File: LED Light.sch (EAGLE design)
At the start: 13 parts, among them J1 AVR_SPI_PRG_6NS, U1 Tiny85-20-SMT

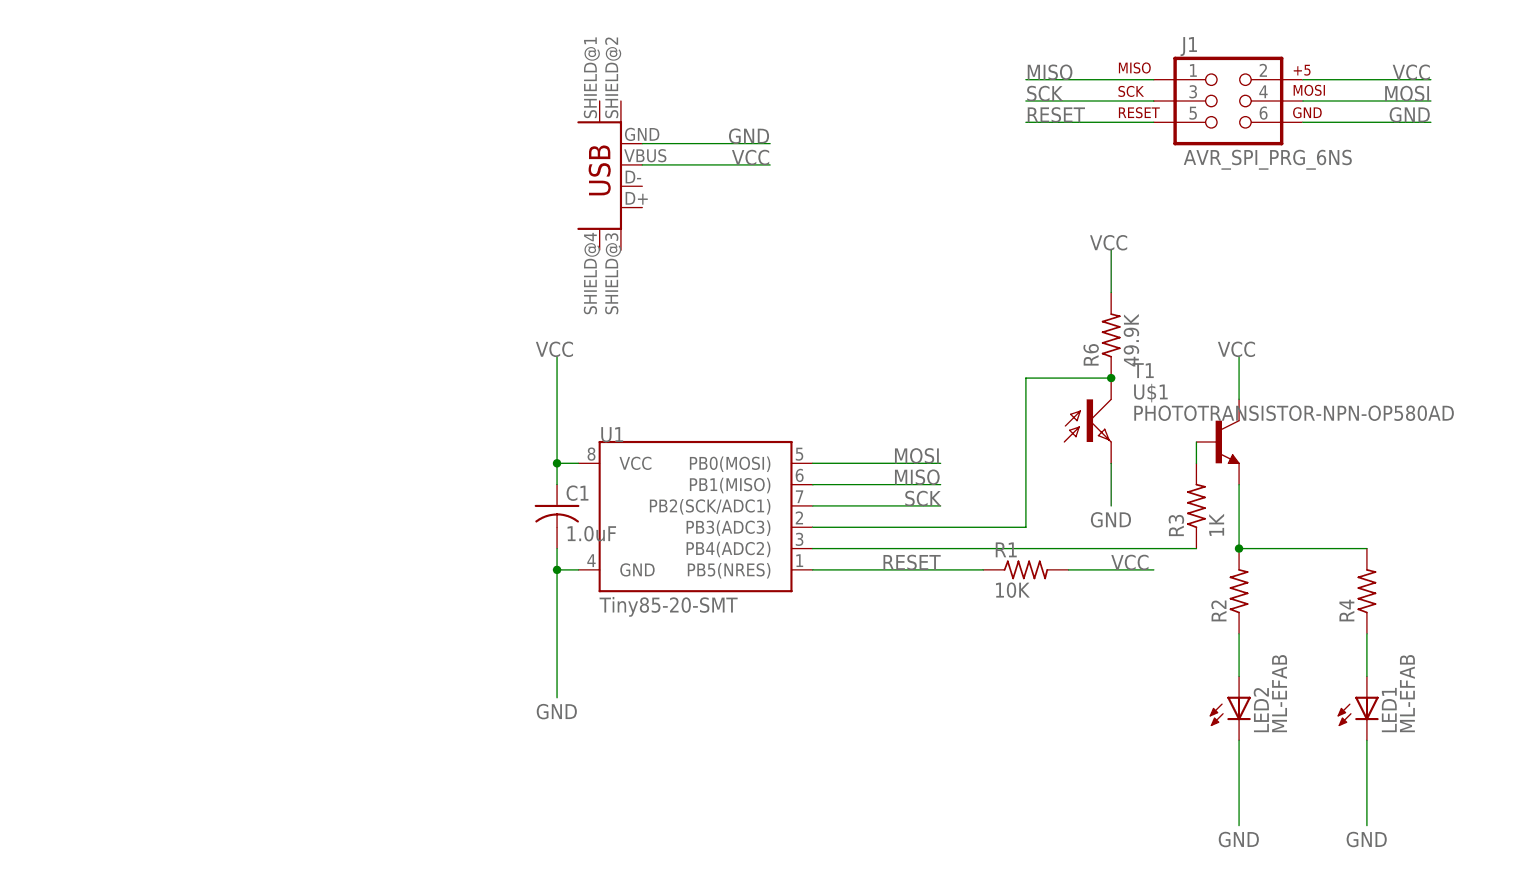
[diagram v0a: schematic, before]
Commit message: Replace Mini-B USB connector w/ male A. Switch LEDs to PB1 (MISO). Layout.
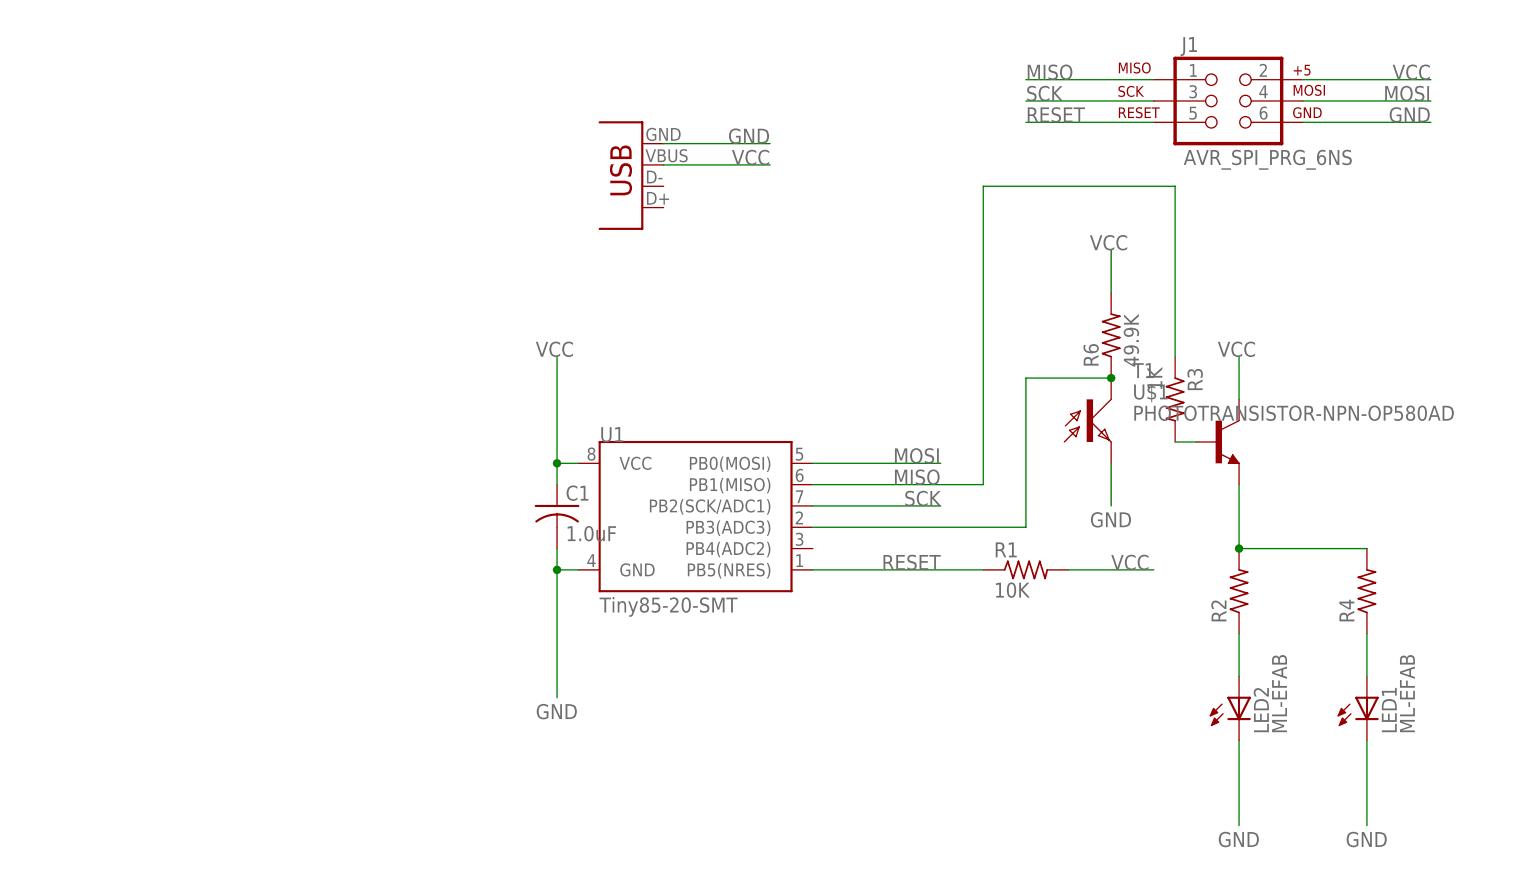
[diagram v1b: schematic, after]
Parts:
- JP1: value USB_MINIB-POWER -> USB_A_VERTICAL; device LED Light:USB_MINIB-POWER -> LED Light:USB_A_VERTICAL
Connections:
- removed net N$4: R3.1, U1.PB4(ADC2)
- net MISO: now also R3.1
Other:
- moved on the sheet: R3
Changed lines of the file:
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@@
 <part name="R1" library="rcl" deviceset="R-US_" device="R1206" value="10K"/>
 <part name="R2" library="rcl" deviceset="R-US_" device="R1206"/>
-<part name="JP1" library="LED Light" deviceset="USB_MINIB" device="-POWER"/>
+<part name="JP1" library="LED Light" deviceset="USB_A_VERTICAL" device=""/>
 <part name="C1" library="rcl" deviceset="C-US" device="C1206" value="1.0uF"/>
 <part name="LED2" library="LED Light" deviceset="ML-E" device="FAB"/>
@@
 <instance part="R1" gate="G$1" x="66.04" y="33.02"/>
 <instance part="R2" gate="G$1" x="91.44" y="30.48" rot="R90"/>
-<instance part="JP1" gate="G$1" x="17.78" y="78.74" rot="R180"/>
+<instance part="JP1" gate="G$1" x="17.78" y="81.28" rot="R180"/>
 <instance part="C1" gate="G$1" x="10.16" y="40.64"/>
 <instance part="LED2" gate="G$1" x="91.44" y="15.24"/>
 <instance part="T1" gate="G$1" x="88.9" y="48.26"/>
-<instance part="R3" gate="G$1" x="86.36" y="40.64" rot="R90"/>
+<instance part="R3" gate="G$1" x="83.82" y="53.34" rot="R270"/>
 <instance part="R4" gate="G$1" x="106.68" y="30.48" rot="R90"/>
 <instance part="LED1" gate="G$1" x="106.68" y="15.24"/>
@@
 <segment>
 <pinref part="JP1" gate="G$1" pin="VBUS"/>
-<wire x1="20.32" y1="81.28" x2="35.56" y2="81.28" width="0.1524" layer="91"/>
+<wire x1="22.86" y1="81.28" x2="35.56" y2="81.28" width="0.1524" layer="91"/>
 <label x="35.56" y="81.28" size="1.778" layer="95" rot="MR0"/>
 </segment>
@@
 <segment>
 <pinref part="JP1" gate="G$1" pin="GND"/>
-<wire x1="20.32" y1="83.82" x2="35.56" y2="83.82" width="0.1524" layer="91"/>
+<wire x1="22.86" y1="83.82" x2="35.56" y2="83.82" width="0.1524" layer="91"/>
 <label x="35.56" y="83.82" size="1.778" layer="95" rot="MR0"/>
 </segment>
@@
 <segment>
 <pinref part="U1" gate="G$1" pin="PB1(MISO)"/>
-<wire x1="40.64" y1="43.18" x2="55.88" y2="43.18" width="0.1524" layer="91"/>
+<wire x1="40.64" y1="43.18" x2="60.96" y2="43.18" width="0.1524" layer="91"/>
 <label x="55.88" y="43.18" size="1.778" layer="95" rot="MR0"/>
+<pinref part="R3" gate="G$1" pin="1"/>
+<wire x1="83.82" y1="58.42" x2="83.82" y2="78.74" width="0.1524" layer="91"/>
+<wire x1="83.82" y1="78.74" x2="60.96" y2="78.74" width="0.1524" layer="91"/>
+<wire x1="60.96" y1="78.74" x2="60.96" y2="43.18" width="0.1524" layer="91"/>
 </segment>
 </net>
@@
 <pinref part="T1" gate="G$1" pin="B"/>
 <pinref part="R3" gate="G$1" pin="2"/>
-<wire x1="86.36" y1="48.26" x2="86.36" y2="45.72" width="0.1524" layer="91"/>
+<wire x1="86.36" y1="48.26" x2="83.82" y2="48.26" width="0.1524" layer="91"/>
 </segment>
 </net>
-<net name="N$4" class="0">
-<segment>
-<pinref part="U1" gate="G$1" pin="PB4(ADC2)"/>
-<pinref part="R3" gate="G$1" pin="1"/>
-<wire x1="40.64" y1="35.56" x2="86.36" y2="35.56" width="0.1524" layer="91"/>
-</segment>
-</net>

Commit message: Board w/ accelerometer and LiPo charging circuit.
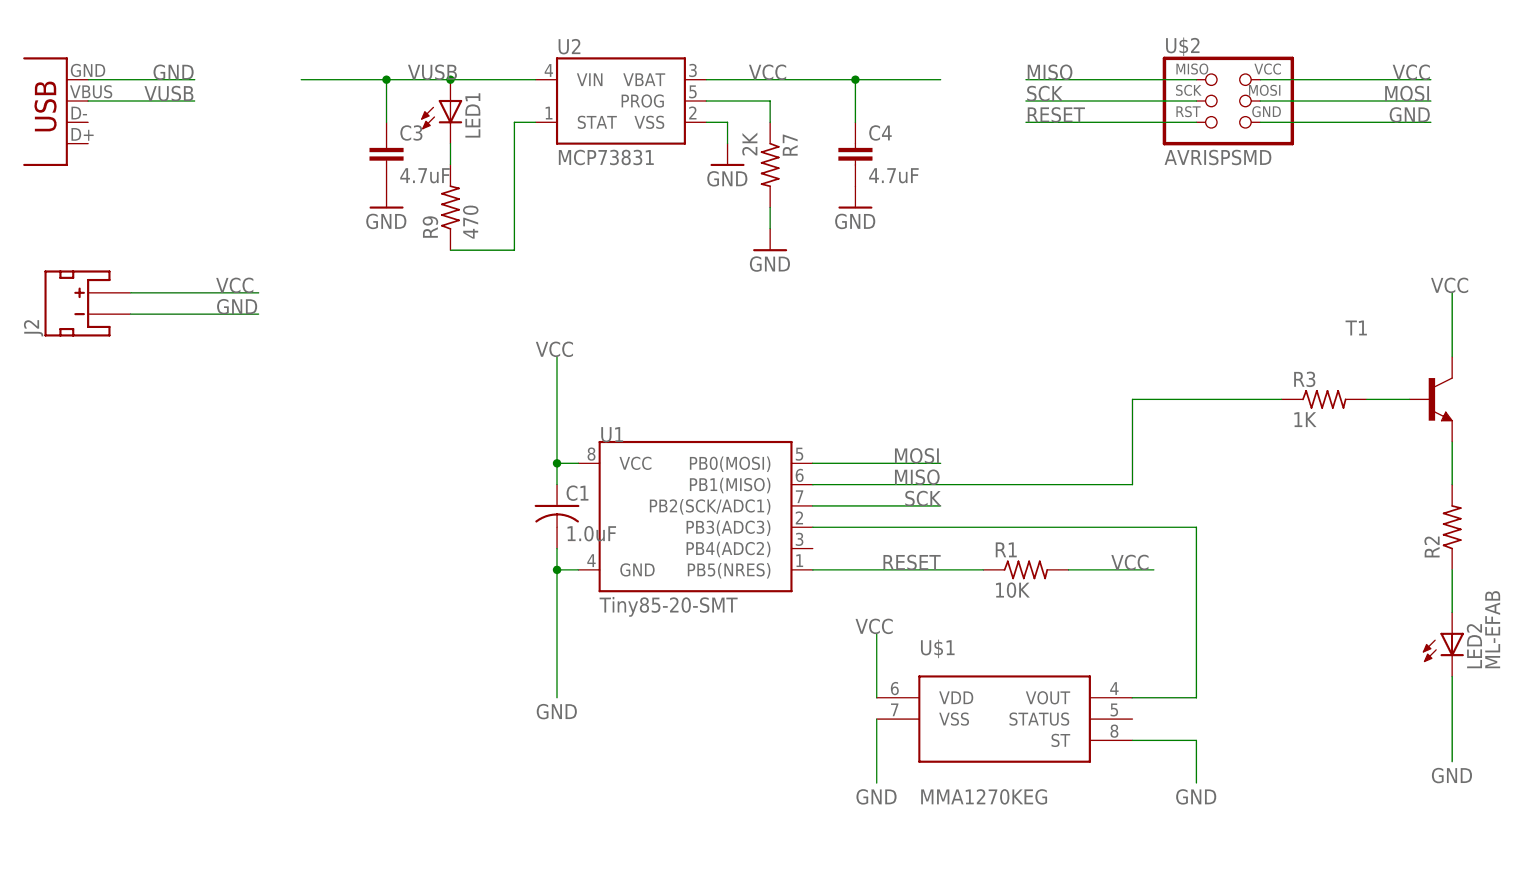
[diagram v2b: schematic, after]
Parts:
- removed J1: AVR_SPI_PRG_6NS, SparkFun-Connectors:AVR_SPI_PRG_6NS
- removed R4: (no value), rcl:R-US_R1206
- removed R6: 49.9K, rcl:R-US_R1206
- added C3, C4: 4.7uF, cellphone-rcl:C-EUC1206
- added J2: (no value), SparkFun-Connectors:JST_2MM_MALE
- added R7: 2K, cellphone-rcl:R-US_R1206
- added R9: 470, cellphone-rcl:R-US_R1206
- added U$2: AVRISPSMD, fab:AVRISPSMD
- added U2: MCP73831, SparkFun:MCP73831
- JP1: value USB_A_VERTICAL -> USB-B-VERTICAL; device LED Light:USB_A_VERTICAL -> LED Light:USB-B-VERTICAL
- LED1: value ML-EFAB -> (none); device LED Light:ML-EFAB -> cellphone-led:LEDSMT1206
- U$1: value PHOTOTRANSISTOR-NPN-OP580AD -> MMA1270KEG; device LED Light:PHOTOTRANSISTOR-NPN-OP580AD -> LED Light:MMA1270KEG
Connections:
- removed net N$5: LED1G$1.A@1, R4.1
- new net N$35: R9.1, U2.STAT
- new net N$36: LED1.C, R9.2
- new net PROG: R7.1, U2.PROG
- new net VUSB: C3.1, JP1.VBUS, LED1.A, U2.VIN
- net GND: now also C3.2, C4.2, J2.-, R7.2, U$1.ST, U$1.VSS, U$2.GND, U2.VSS; no longer J1.6, LED1G$1.C@1, U$1.E
- net MISO: now also U$2.MISO; no longer J1.1
- net MOSI: now also U$2.MOSI; no longer J1.4
- net N$1: no longer R4.2
- net N$7: now also U$1.VOUT; no longer R6.1, U$1.C
- net RESET: now also U$2.RST; no longer J1.5
- net SCK: now also U$2.SCK; no longer J1.3
- net VCC: now also C4.1, J2.+, U$1.VDD, U$2.VCC, U2.VBAT; no longer J1.2, JP1.VBUS, R6.2
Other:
- moved on the sheet: LED2, R2, R3, T1

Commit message: Replace non-standard parts, two-sided layout, silk
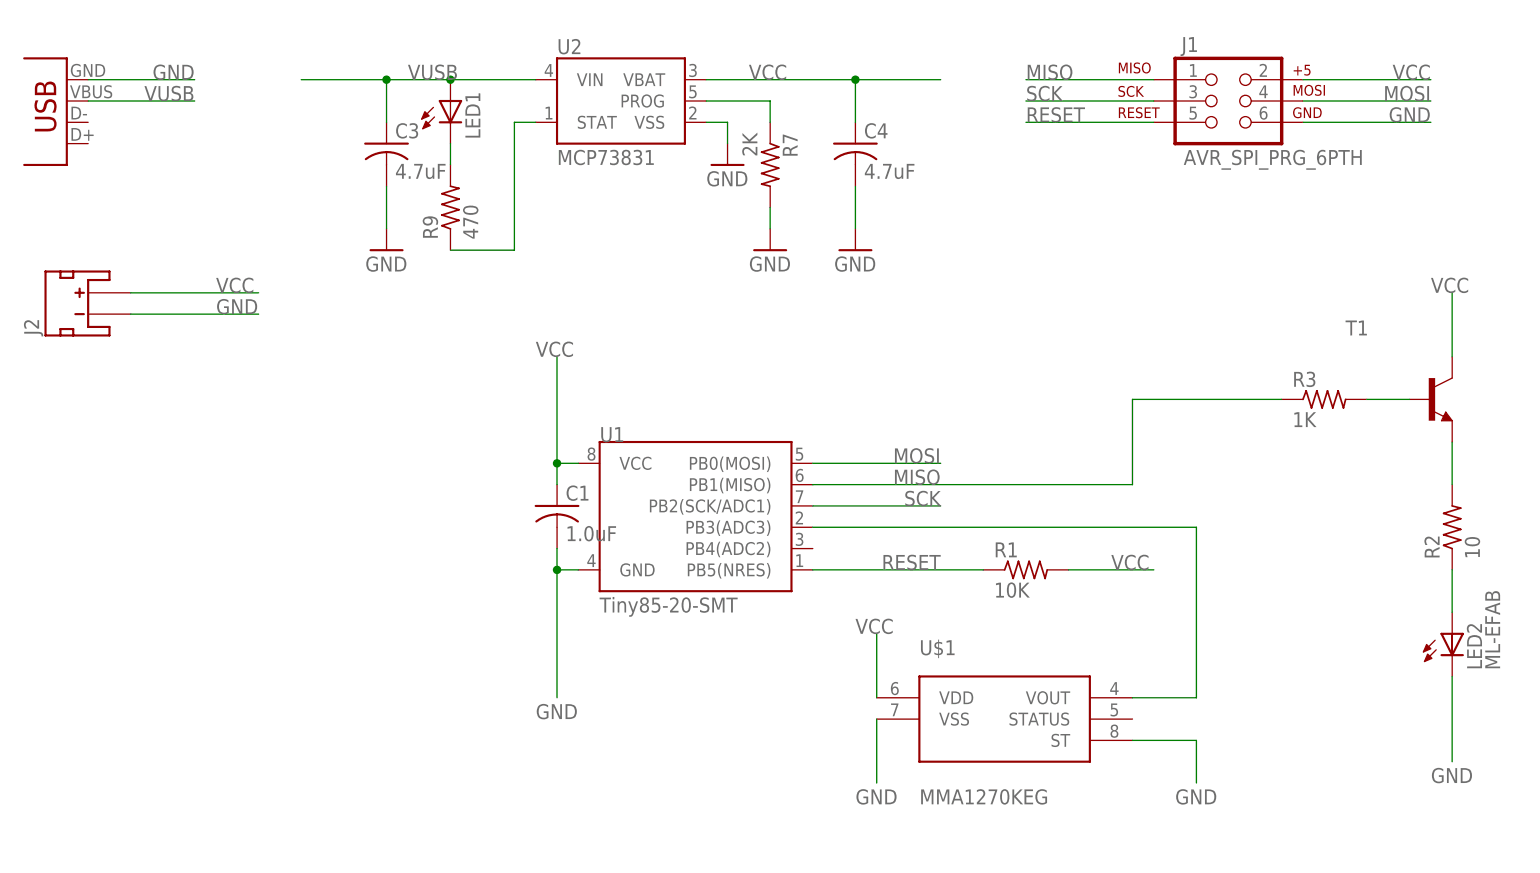
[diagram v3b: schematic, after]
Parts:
- removed U$2: AVRISPSMD, fab:AVRISPSMD
- added J1: AVR_SPI_PRG_6PTH, SparkFun-Connectors:AVR_SPI_PRG_6PTH
- C3, C4: device cellphone-rcl:C-EUC1206 -> rcl:C-USC1206
- R2: value (none) -> 10
- R7, R9: device cellphone-rcl:R-US_R1206 -> rcl:R-US_R1206
- U2: device SparkFun:MCP73831 -> SparkFun-PowerIC:MCP73831
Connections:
- net GND: now also J1.6; no longer U$2.GND
- net MISO: now also J1.1; no longer U$2.MISO
- net MOSI: now also J1.4; no longer U$2.MOSI
- net RESET: now also J1.5; no longer U$2.RST
- net SCK: now also J1.3; no longer U$2.SCK
- net VCC: now also J1.2; no longer U$2.VCC
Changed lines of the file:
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@@
 <class number="0" name="default" width="0" drill="0">
 </class>
-<class number="1" name="power" width="0.254" drill="0.4064">
-<clearance class="1" value="0.1778"/>
-</class>
-<class number="2" name="gnd" width="0.254" drill="0.4064">
-<clearance class="2" value="0.1778"/>
+<class number="1" name="power" width="0.4064" drill="0">
 </class>
 </classes>
@@
 <part name="U1" library="SparkFun-DigitalIC" deviceset="ATTINY45" device="TINY85-20-SMT" value="Tiny85-20-SMT"/>
 <part name="R1" library="rcl" deviceset="R-US_" device="R1206" value="10K"/>
-<part name="R2" library="rcl" deviceset="R-US_" device="R1206"/>
+<part name="R2" library="rcl" deviceset="R-US_" device="R1206" value="10"/>
 <part name="JP1" library="LED Light" deviceset="USB" device="-B-VERTICAL"/>
 <part name="C1" library="rcl" deviceset="C-US" device="C1206" value="1.0uF"/>
@@
 <part name="GND17" library="SparkFun" deviceset="GND" device=""/>
 <part name="GND18" library="SparkFun" deviceset="GND" device=""/>
-<part name="U2" library="SparkFun" deviceset="MCP73831" device=""/>
-<part name="R7" library="cellphone-rcl" deviceset="R-US_" device="R1206" value="2K"/>
+<part name="U2" library="SparkFun-PowerIC" deviceset="MCP73831" device=""/>
+<part name="R7" library="rcl" deviceset="R-US_" device="R1206" value="2K"/>
 <part name="GND19" library="SparkFun" deviceset="GND" device=""/>
-<part name="C3" library="cellphone-rcl" deviceset="C-EU" device="C1206" value="4.7uF"/>
-<part name="C4" library="cellphone-rcl" deviceset="C-EU" device="C1206" value="4.7uF"/>
-<part name="R9" library="cellphone-rcl" deviceset="R-US_" device="R1206" value="470"/>
+<part name="C3" library="rcl" deviceset="C-US" device="C1206" value="4.7uF"/>
+<part name="C4" library="rcl" deviceset="C-US" device="C1206" value="4.7uF"/>
+<part name="R9" library="rcl" deviceset="R-US_" device="R1206" value="470"/>
 <part name="LED1" library="cellphone-led" deviceset="LED" device="SMT1206"/>
 <part name="J2" library="SparkFun-Connectors" deviceset="JST_2MM_MALE" device=""/>
-<part name="U$2" library="fab" deviceset="AVRISP" device="SMD"/>
+<part name="J1" library="SparkFun-Connectors" deviceset="AVR_SPI_PRG_6" device="PTH"/>
 </parts>
 <sheets>
@@
 <instance part="R3" gate="G$1" x="101.6" y="53.34"/>
 <instance part="U$1" gate="G$1" x="63.5" y="15.24"/>
-<instance part="GND14" gate="1" x="45.72" y="76.2"/>
-<instance part="GND17" gate="1" x="-10.16" y="76.2"/>
+<instance part="GND14" gate="1" x="45.72" y="71.12"/>
+<instance part="GND17" gate="1" x="-10.16" y="71.12"/>
 <instance part="GND18" gate="1" x="30.48" y="81.28"/>
 <instance part="U2" gate="G$1" x="17.78" y="88.9"/>
@@
 <instance part="LED1" gate="G$1" x="-2.54" y="88.9"/>
 <instance part="J2" gate="G$1" x="-45.72" y="63.5" rot="R90"/>
-<instance part="U$2" gate="G$1" x="88.9" y="88.9"/>
+<instance part="J1" gate="G$1" x="88.9" y="88.9"/>
 </instances>
 <busses>
 </busses>
 <nets>
-<net name="VCC" class="0">
-<segment>
-<wire x1="93.98" y1="91.44" x2="114.3" y2="91.44" width="0.1524" layer="91"/>
+<net name="VCC" class="1">
+<segment>
+<wire x1="99.06" y1="91.44" x2="114.3" y2="91.44" width="0.1524" layer="91"/>
 <label x="114.3" y="91.44" size="1.778" layer="95" rot="MR0"/>
-<pinref part="U$2" gate="G$1" pin="VCC"/>
+<pinref part="J1" gate="G$1" pin="2"/>
 </segment>
 <segment>
@@
 <net name="MOSI" class="0">
 <segment>
-<wire x1="93.98" y1="88.9" x2="114.3" y2="88.9" width="0.1524" layer="91"/>
+<wire x1="99.06" y1="88.9" x2="114.3" y2="88.9" width="0.1524" layer="91"/>
 <label x="114.3" y="88.9" size="1.778" layer="95" rot="MR0"/>
-<pinref part="U$2" gate="G$1" pin="MOSI"/>
+<pinref part="J1" gate="G$1" pin="4"/>
 </segment>
 <segment>
@@
 </segment>
 </net>
-<net name="GND" class="0">
-<segment>
-<wire x1="93.98" y1="86.36" x2="114.3" y2="86.36" width="0.1524" layer="91"/>
+<net name="GND" class="1">
+<segment>
+<wire x1="99.06" y1="86.36" x2="114.3" y2="86.36" width="0.1524" layer="91"/>
 <label x="114.3" y="86.36" size="1.778" layer="95" rot="MR0"/>
-<pinref part="U$2" gate="G$1" pin="GND"/>
+<pinref part="J1" gate="G$1" pin="6"/>
 </segment>
 <segment>
@@
 <pinref part="GND14" gate="1" pin="GND"/>
 <pinref part="C4" gate="G$1" pin="2"/>
+<wire x1="45.72" y1="73.66" x2="45.72" y2="78.74" width="0.1524" layer="91"/>
 </segment>
 <segment>
 <pinref part="GND17" gate="1" pin="GND"/>
 <pinref part="C3" gate="G$1" pin="2"/>
+<wire x1="-10.16" y1="73.66" x2="-10.16" y2="78.74" width="0.1524" layer="91"/>
 </segment>
 <segment>
@@
 <net name="RESET" class="0">
 <segment>
-<wire x1="86.36" y1="86.36" x2="66.04" y2="86.36" width="0.1524" layer="91"/>
 <label x="66.04" y="86.36" size="1.778" layer="95"/>
-<pinref part="U$2" gate="G$1" pin="RST"/>
+<pinref part="J1" gate="G$1" pin="5"/>
+<wire x1="81.28" y1="86.36" x2="66.04" y2="86.36" width="0.1524" layer="91"/>
 </segment>
 <segment>
@@
 <net name="SCK" class="0">
 <segment>
-<wire x1="86.36" y1="88.9" x2="66.04" y2="88.9" width="0.1524" layer="91"/>
 <label x="66.04" y="88.9" size="1.778" layer="95"/>
-<pinref part="U$2" gate="G$1" pin="SCK"/>
+<pinref part="J1" gate="G$1" pin="3"/>
+<wire x1="81.28" y1="88.9" x2="66.04" y2="88.9" width="0.1524" layer="91"/>
 </segment>
 <segment>
@@
 <net name="MISO" class="0">
 <segment>
-<wire x1="86.36" y1="91.44" x2="66.04" y2="91.44" width="0.1524" layer="91"/>
 <label x="66.04" y="91.44" size="1.778" layer="95"/>
-<pinref part="U$2" gate="G$1" pin="MISO"/>
+<pinref part="J1" gate="G$1" pin="1"/>
+<wire x1="81.28" y1="91.44" x2="66.04" y2="91.44" width="0.1524" layer="91"/>
 </segment>
 <segment>
@@
 </segment>
 </net>
-<net name="VUSB" class="0">
+<net name="VUSB" class="1">
 <segment>
 <wire x1="-10.16" y1="86.36" x2="-10.16" y2="91.44" width="0.1524" layer="91"/>
